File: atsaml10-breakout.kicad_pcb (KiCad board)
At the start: 2 copper layers, 24.4 x 50.8 mm, 40 parts, among them J1 Conn_01x16, J2 Conn_01x16, J3 SWD, Q1 BC847, Q2 BC847, SW1 Reset, U1 ATSAML10E16A-A, Y1 32.768kHz, Y2 8MHz

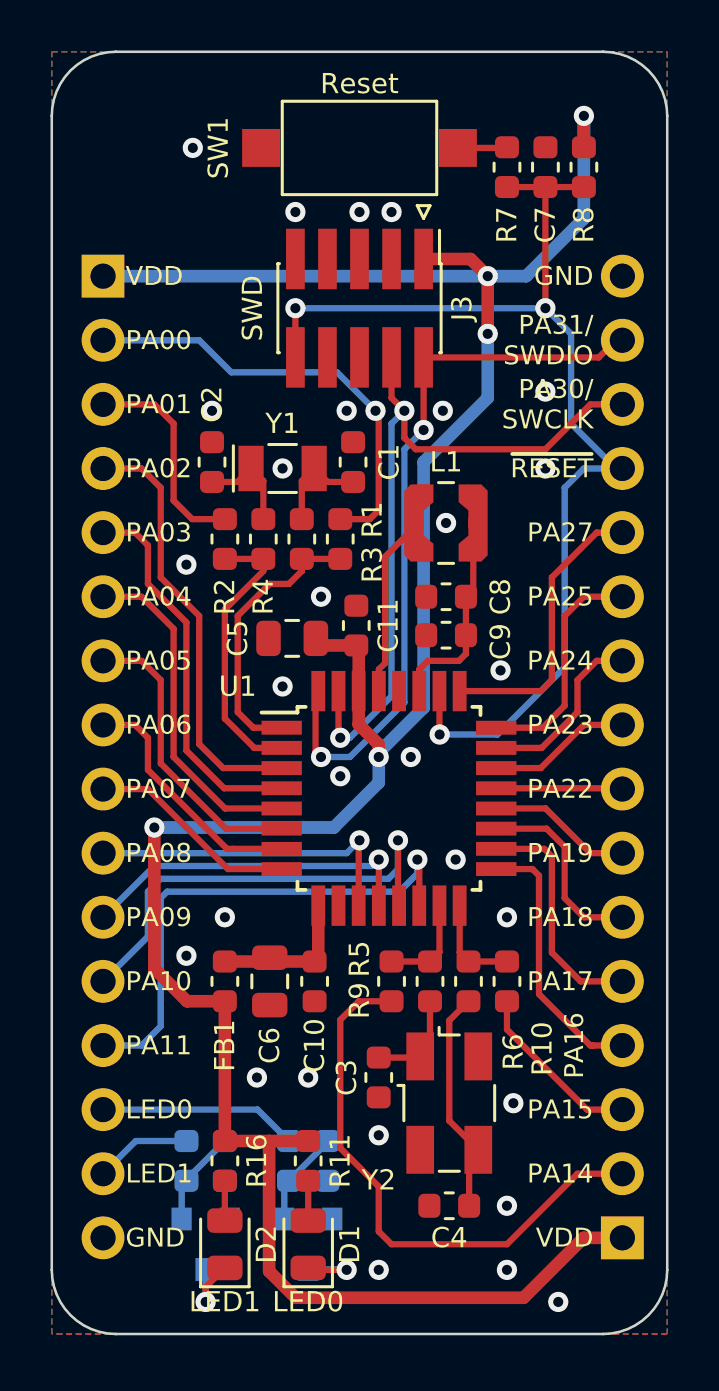
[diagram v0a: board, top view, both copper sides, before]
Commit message: Schematic cleanup, more PCB tweaks
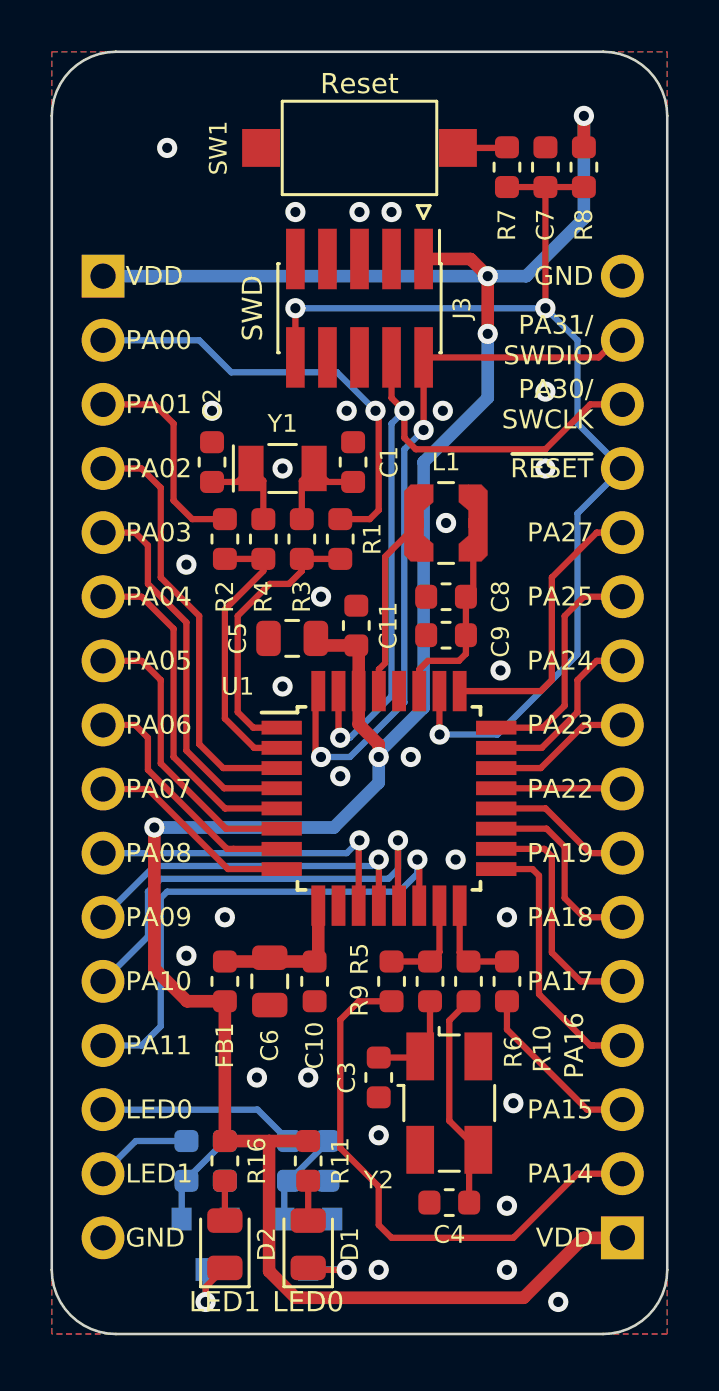
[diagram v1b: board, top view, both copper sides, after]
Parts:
- added REF**: OSHW-Logo_5.7x6mm_SilkScreen, Symbol:OSHW-Logo_5.7x6mm_SilkScreen, B.Cu at (161.0, 80.0)
- J1: value Conn_01x16 -> Left
- J2: value Conn_01x16 -> Right
- L1: value 10uH -> LPS3015-103MRB
- R1, R10, R2, R9: value DNP -> 0R
- moved C4 0.13 mm to (156.0, 121.8)
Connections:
- net Net-(J2-Pad2) renamed /PA14
- net Net-(J2-Pad3) renamed /PA15
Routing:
- net /~RESET: track 44.5 -> 43.9 mm
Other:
- board text added: "ATSAML10 Breakout Board © 2020 Michal Potrzebicz michal@elevendroids.com CC BY-SA 4.0"
- board text added: "Rev. A"

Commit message: PCB size tweaks, align headers to 0.1" grid
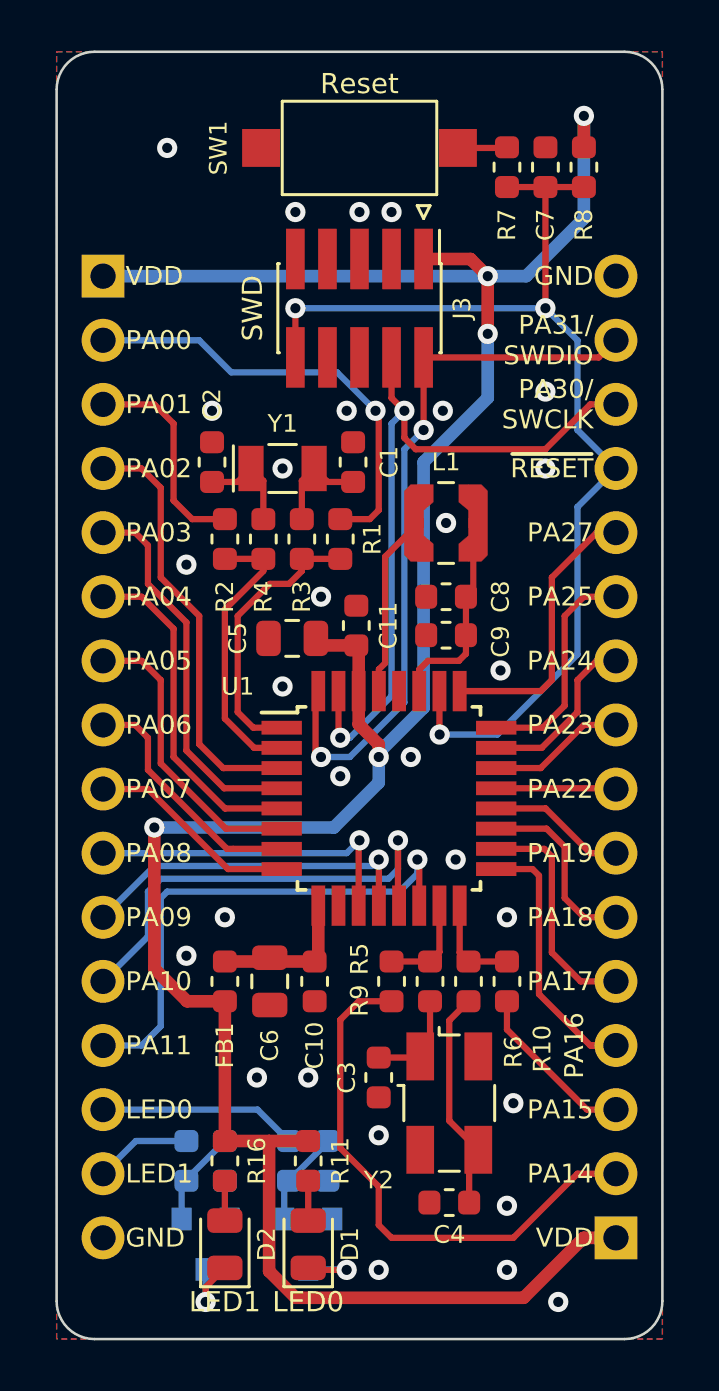
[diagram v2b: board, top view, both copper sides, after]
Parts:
- moved J2 0.25 mm to (162.6, 123.2)
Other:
- board size 24.4 x 50.8 mm -> 24 x 51 mm
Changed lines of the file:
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@@
   (general
     (thickness 1.6)
-    (drawings 45)
+    (drawings 47)
     (tracks 321)
     (zones 0)
@@
     (user_trace_width 0.75)
     (trace_clearance 0.2)
-    (zone_clearance 0.1524)
+    (zone_clearance 0.2)
     (zone_45_only no)
     (trace_min 0.2)
@@
   )
   (module Connector_PinHeader_2.54mm:PinHeader_1x16_P2.54mm_Vertical (layer B.Cu)
-    (at 162.814 123.19)
+    (at 162.56 123.19)
     (descr "Through hole straight pin header, 1x16, 2.54mm pitch, single row")
     (tags "Through hole pin header THT 1x16 2.54mm single row")
@@
     )
   )
+  (dimension 51 (width 0.15) (layer Dwgs.User)
+    (gr_text "51.000 mm" (at 168.3 101.7 270) (layer Dwgs.User)
+      (effects (font (size 1 1) (thickness 0.15)))
+    )
+    (feature1 (pts (xy 162.9 127.2) (xy 167.586421 127.2)))
+    (feature2 (pts (xy 162.9 76.2) (xy 167.586421 76.2)))
+    (crossbar (pts (xy 167 76.2) (xy 167 127.2)))
+    (arrow1a (pts (xy 167 127.2) (xy 166.413579 126.073496)))
+    (arrow1b (pts (xy 167 127.2) (xy 167.586421 126.073496)))
+    (arrow2a (pts (xy 167 76.2) (xy 166.413579 77.326504)))
+    (arrow2b (pts (xy 167 76.2) (xy 167.586421 77.326504)))
+  )
+  (gr_arc (start 162.9 77.7) (end 164.4 77.7) (angle -90) (layer Edge.Cuts) (width 0.1))
+  (gr_arc (start 162.9 125.7) (end 162.9 127.2) (angle -90) (layer Edge.Cuts) (width 0.1))
+  (gr_arc (start 141.9 125.7) (end 140.4 125.7) (angle -90) (layer Edge.Cuts) (width 0.1))
+  (gr_arc (start 141.9 77.7) (end 141.9 76.2) (angle -90) (layer Edge.Cuts) (width 0.1))
+  (dimension 24 (width 0.15) (layer Dwgs.User)
+    (gr_text "24.000 mm" (at 152.4 70.2) (layer Dwgs.User)
+      (effects (font (size 1 1) (thickness 0.15)))
+    )
+    (feature1 (pts (xy 164.4 77.7) (xy 164.4 70.913579)))
+    (feature2 (pts (xy 140.4 77.7) (xy 140.4 70.913579)))
+    (crossbar (pts (xy 140.4 71.5) (xy 164.4 71.5)))
+    (arrow1a (pts (xy 164.4 71.5) (xy 163.273496 72.086421)))
+    (arrow1b (pts (xy 164.4 71.5) (xy 163.273496 70.913579)))
+    (arrow2a (pts (xy 140.4 71.5) (xy 141.526504 72.086421)))
+    (arrow2b (pts (xy 140.4 71.5) (xy 141.526504 70.913579)))
+  )
   (gr_text "Rev. A" (at 157.734 125.73) (layer B.SilkS)
     (effects (font (size 0.8 0.8) (thickness 0.15)) (justify mirror))
@@
     (effects (font (size 0.75 0.75) (thickness 0.15)) (justify left))
   )
-  (gr_arc (start 162.052 124.46) (end 162.052 127) (angle -90) (layer Edge.Cuts) (width 0.1016))
-  (gr_arc (start 142.748 124.46) (end 140.208 124.46) (angle -90) (layer Edge.Cuts) (width 0.1016))
-  (gr_arc (start 142.748 78.74) (end 142.748 76.2) (angle -90) (layer Edge.Cuts) (width 0.1016))
-  (gr_arc (start 162.052 78.74) (end 164.592 78.74) (angle -90) (layer Edge.Cuts) (width 0.1016))
-  (gr_line (start 140.208 124.46) (end 140.208 78.74) (layer Edge.Cuts) (width 0.1016))
-  (gr_line (start 162.052 127) (end 142.748 127) (layer Edge.Cuts) (width 0.1016))
-  (gr_line (start 164.592 78.74) (end 164.592 124.46) (layer Edge.Cuts) (width 0.1016))
-  (gr_line (start 142.748 76.2) (end 162.052 76.2) (layer Edge.Cuts) (width 0.1016))
+  (gr_line (start 140.4 125.7) (end 140.4 77.7) (layer Edge.Cuts) (width 0.1016))
+  (gr_line (start 162.9 127.2) (end 141.9 127.2) (layer Edge.Cuts) (width 0.1016))
+  (gr_line (start 164.4 77.7) (end 164.4 125.7) (layer Edge.Cuts) (width 0.1016))
+  (gr_line (start 141.9 76.2) (end 162.9 76.2) (layer Edge.Cuts) (width 0.1016))
   (segment (start 150.114 93.198) (end 150.602 92.71) (width 0.25) (layer F.Cu) (net 1))
   (segment (start 150.114 94.7165) (end 150.114 93.198) (width 0.25) (layer F.Cu) (net 1))
@@
   (segment (start 155.567522 103.243522) (end 155.575 103.251) (width 0.25) (layer F.Cu) (net 8))
   (segment (start 155.567522 101.529303) (end 155.567522 103.243522) (width 0.25) (layer F.Cu) (net 8))
+  (segment (start 161.036 94.234) (end 162.56 92.71) (width 0.25) (layer B.Cu) (net 8))
+  (segment (start 161.036 100.076) (end 161.036 94.234) (width 0.25) (layer B.Cu) (net 8))
+  (segment (start 157.861 103.251) (end 161.036 100.076) (width 0.25) (layer B.Cu) (net 8))
+  (segment (start 155.575 103.251) (end 157.861 103.251) (width 0.25) (layer B.Cu) (net 8))
   (segment (start 161.036 87.63) (end 159.766 86.36) (width 0.25) (layer B.Cu) (net 8))
-  (segment (start 161.036 90.932) (end 161.036 87.63) (width 0.25) (layer B.Cu) (net 8))
-  (segment (start 162.814 92.71) (end 161.036 90.932) (width 0.25) (layer B.Cu) (net 8))
-  (segment (start 157.861 103.251) (end 155.575 103.251) (width 0.25) (layer B.Cu) (net 8))
-  (segment (start 161.036 100.076) (end 157.861 103.251) (width 0.25) (layer B.Cu) (net 8))
-  (segment (start 161.036 94.488) (end 161.036 100.076) (width 0.25) (layer B.Cu) (net 8))
-  (segment (start 161.036 94.488) (end 162.814 92.71) (width 0.25) (layer B.Cu) (net 8))
+  (segment (start 161.036 91.186) (end 161.036 87.63) (width 0.25) (layer B.Cu) (net 8))
+  (segment (start 162.56 92.71) (end 161.036 91.186) (width 0.25) (layer B.Cu) (net 8))
   (segment (start 156.909 97.4975) (end 156.6165 97.79) (width 0.25) (layer F.Cu) (net 9))
   (segment (start 156.909 94.869) (end 156.909 97.4975) (width 0.25) (layer F.Cu) (net 9))
@@
   (segment (start 162.56 120.65) (end 161.036 120.65) (width 0.25) (layer F.Cu) (net 51))
   (zone (net 2) (net_name GND) (layer F.Cu) (hatch edge 0.508)
-    (connect_pads (clearance 0.1524))
-    (min_thickness 0.1524)
-    (fill yes (arc_segments 32) (thermal_gap 0.1524) (thermal_bridge_width 0.2032))
+    (connect_pads (clearance 0.2))
+    (min_thickness 0.16)
+    (fill yes (arc_segments 32) (thermal_gap 0.2) (thermal_bridge_width 0.381))
     (polygon
       (pts
-        (xy 164.592 127) (xy 140.208 127) (xy 140.208 76.2) (xy 164.592 76.2)
+        (xy 164.4 127.2) (xy 140.4 127.2) (xy 140.4 76.2) (xy 164.4 76.2)
       )
     )
   )
   (zone (net 2) (net_name GND) (layer B.Cu) (hatch edge 0.508)
-    (connect_pads (clearance 0.1524))
-    (min_thickness 0.1524)
-    (fill yes (arc_segments 32) (thermal_gap 0.1524) (thermal_bridge_width 0.2032))
+    (connect_pads (clearance 0.2))
+    (min_thickness 0.16)
+    (fill yes (arc_segments 32) (thermal_gap 0.2) (thermal_bridge_width 0.381))
     (polygon
       (pts
-        (xy 164.592 127) (xy 140.208 127) (xy 140.208 76.2) (xy 164.592 76.2)
+        (xy 164.4 127.2) (xy 140.4 127.2) (xy 140.4 76.2) (xy 164.4 76.2)
       )
     )

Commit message: Getting revision A ready
- Replaced Q1 and Q2 with BC847BDW1 and moved the chip to the front
  layer
- Replaced 0R resistors' packages with 0402
- Filled MFR and MPN fields for some parts
- Added DNP fields for the option jumpers
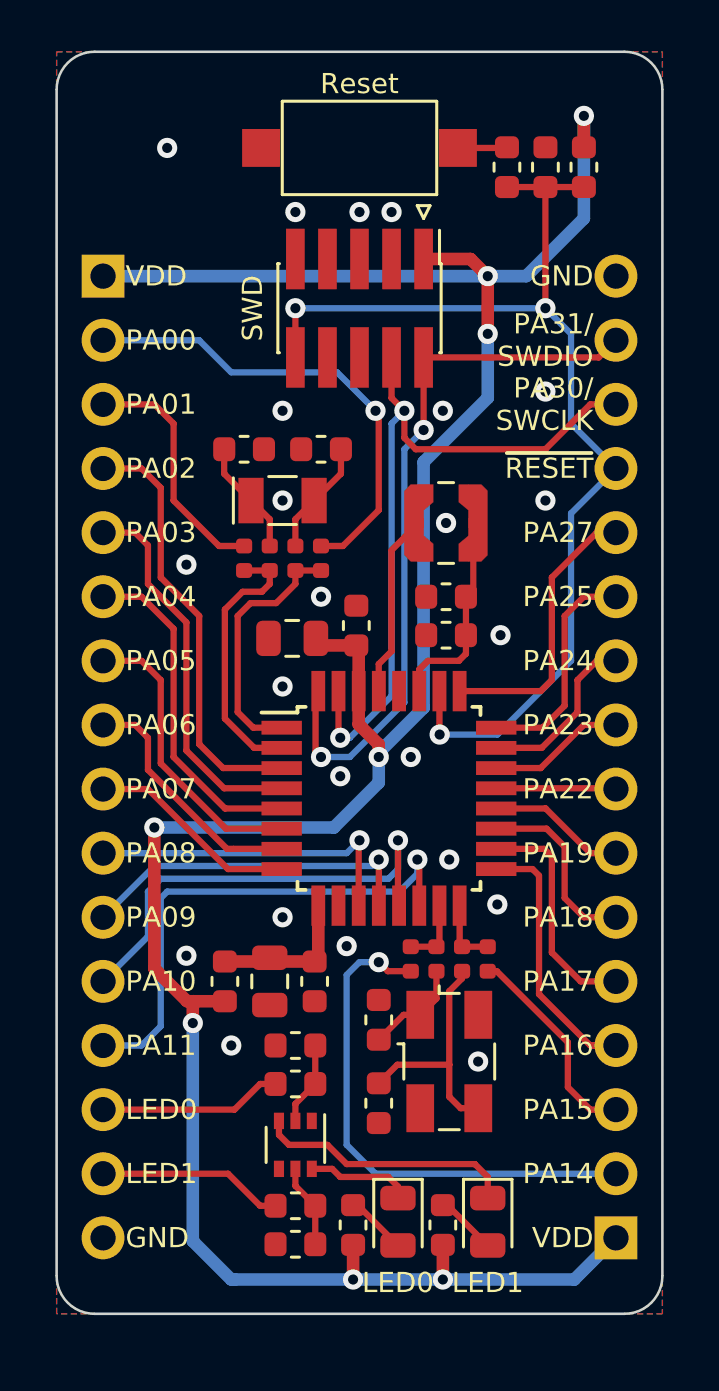
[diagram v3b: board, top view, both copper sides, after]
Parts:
- removed Q2: BC847, Package_TO_SOT_SMD:SOT-23
- FB1: value BLM18AG221SN1D -> 220R/100MHz
- L1: value LPS3015-103MRB -> 10uH
- Q1: value BC847 -> BC847BDW1; footprint Package_TO_SOT_SMD:SOT-23 -> Package_TO_SOT_SMD:SOT-363_SC-70-6; moved to F.Cu
- R1, R10, R2, R3, R4, R5, R6, R9: footprint Resistor_SMD:R_0603_1608Metric -> Resistor_SMD:R_0402_1005Metric
- R12, R13, R14, R15: moved to F.Cu
- moved D2 10.5 mm to (157.5, 122.6), turned to 270 degrees
- moved R16 9.00 mm to (155.7, 122.7), turned to 90 degrees
- moved C4 4.83 mm to (153.2, 117.9), turned to 270 degrees
- moved R14 4.75 mm to (149.9, 115.6), turned to 180 degrees
- moved R13 4.67 mm to (149.9, 121.9), turned to 180 degrees
- moved R15 4.33 mm to (149.9, 123.4), turned to 180 degrees
- moved Q1 3.97 mm to (149.9, 119.5)
- moved D1 3.67 mm to (153.9, 122.6), turned to 270 degrees
- moved R11 3.10 mm to (152.1, 122.7), turned to 90 degrees
- moved R12 3.06 mm to (149.9, 117.1), turned to 180 degrees
- moved C3 2.28 mm to (153.2, 114.6), turned to 270 degrees
- moved Y2 1.65 mm to (156.0, 116.2)
- moved C2 1.37 mm to (147.8, 91.9), turned to 0 degrees
- moved C1 1.37 mm to (150.9, 91.9), turned to 0 degrees
- moved Y1 1.27 mm to (149.4, 94.0)
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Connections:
- Q1 pad 1: Net-(Q1-Pad1) -> GND
- Q1 pad 2: GND -> Net-(Q1-Pad2)
- Q1 pad 3: Net-(D1-Pad1) -> Net-(D2-Pad1)
- R12 pad 1: Net-(Q1-Pad1) -> Net-(Q1-Pad2)
- R13 pad 1: Net-(Q2-Pad1) -> Net-(Q1-Pad5)
- R14 pad 1: Net-(Q1-Pad1) -> Net-(Q1-Pad2)
- R15 pad 1: Net-(Q2-Pad1) -> Net-(Q1-Pad5)
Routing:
- net Net-(D2-Pad1): track 2.95 -> 10.4 mm, vias 1 -> 0
- net Net-(Q2-Pad1): track 3.80 -> 0.00 mm
- net Net-(Q1-Pad1): track 3.80 -> 0.00 mm
- net /LED1: track 3.84 -> 7.36 mm
- net Net-(Q1-Pad5): track 0.00 -> 3.31 mm
- net Net-(Q1-Pad2): track 0.00 -> 3.31 mm
- net /PA15: track 6.75 -> 8.39 mm
- net /PA01: track 8.49 -> 9.70 mm
- net /PA00: track 17.6 -> 18.8 mm
- net /PA15_XOUT: track 3.88 -> 2.68 mm
- net /PA14_XOSC: track 3.89 -> 2.69 mm
- net VDD: track 104.2 -> 105.4 mm, vias 5 -> 8
- net Net-(D1-Pad1): track 3.09 -> 4.16 mm, vias 1 -> 0
- net /PA14: track 21.8 -> 20.8 mm, vias 0 -> 1
- net /PA00_XIN32: track 11.1 -> 10.2 mm
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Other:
- board size 24 x 51 mm -> 24 x 50 mm
- rule pad_to_mask_clearance: 0.05 -> 0.0508
- board text added: "ATSAML1x Breakout Board © 2020 Michal Potrzebicz michal@elevendroids.com CC BY-SA 4.0 Rev. A"
- board text removed: "ATSAML10 Breakout Board © 2020 Michal Potrzebicz michal@elevendroids.com CC BY-SA 4.0"
- board text removed: "Rev. A"

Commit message: Replaced Y2 footprint with a generic one
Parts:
- Y2: footprint Crystal:Crystal_SMD_EuroQuartz_MJ-4Pin_5.0x3.2mm -> Crystal:Crystal_SMD_5032-4Pin_5.0x3.2mm
- moved C4 0.38 mm to (153.2, 117.5)
- moved Y2 0.25 mm to (156.0, 116.0)
- moved C3 0.13 mm to (153.2, 114.4)
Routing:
- net Net-(C4-Pad1): track 9.62 -> 8.65 mm

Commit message: Replaced Y1 footprint with a generic one
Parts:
- Y1: footprint Crystal:Crystal_SMD_EuroQuartz_EQ161-2Pin_3.2x1.5mm -> Crystal:Crystal_SMD_3215-2Pin_3.2x1.5mm
- turned Y1 to 180 degrees

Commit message: Project upgrade to KiCad 6
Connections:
- net /~RESET renamed /~{RESET}
- J3 pad 6: Net-(J3-Pad6) -> unconnected-(J3-Pad6)
- J3 pad 7: Net-(J3-Pad7) -> unconnected-(J3-Pad7)
- J3 pad 8: Net-(J3-Pad8) -> unconnected-(J3-Pad8)
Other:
- net class Default removed
- net class Power removed
- board text added: "~{RESET}"
- board text removed: "~RESET"
